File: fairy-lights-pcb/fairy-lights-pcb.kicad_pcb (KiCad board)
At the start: 2 copper layers, 59.5 x 59 mm, 16 parts, among them J1 Power_Jack, J2 Conn_LED_Strand, J3 Conn_LED_Strand, J4 Conn_Misc, J5 Conn_02x04_Top_Bottom, SW1 SW_PWR, SW2 SW_User, U1 WeMos_D1_mini, U2 TXS0108EPW

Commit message: Connect barrel jack mounting pin to ground
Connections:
- J1 pad 3: unconnected-(J1-MP-Pad3) -> GND

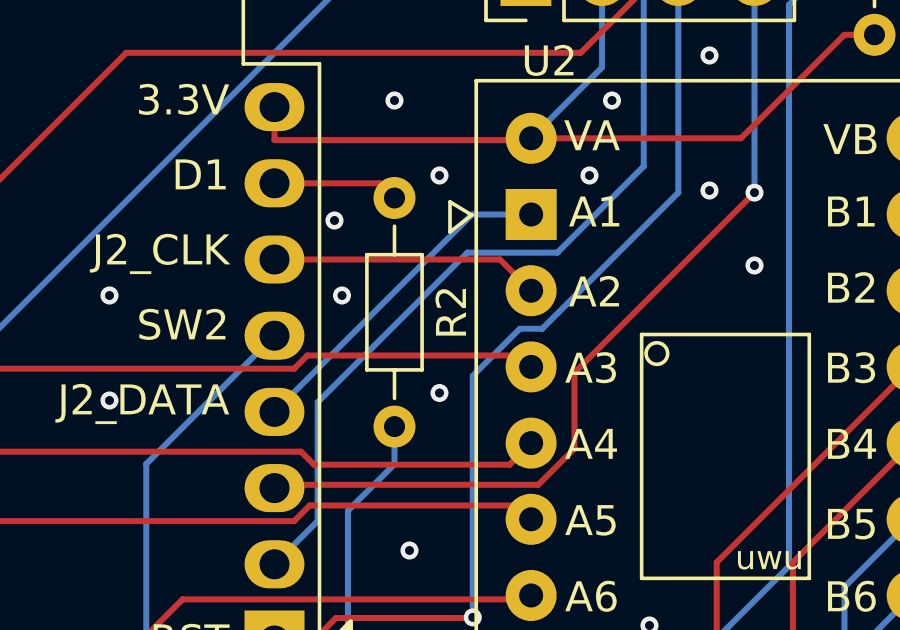
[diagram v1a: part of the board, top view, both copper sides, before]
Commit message: Update user LED resistor value
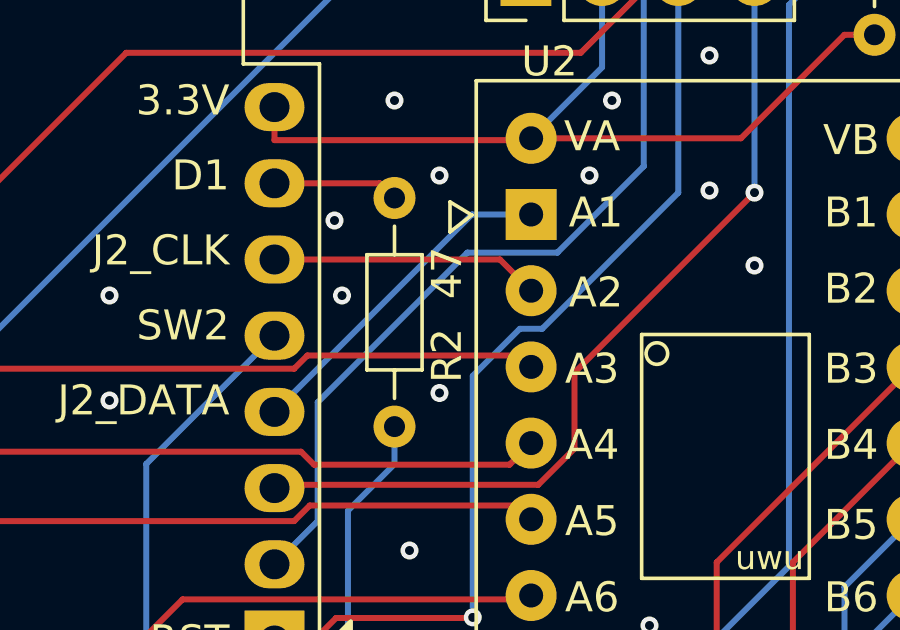
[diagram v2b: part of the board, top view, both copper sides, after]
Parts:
- R2: value TBD -> 47
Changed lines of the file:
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@@
 		(tags "Resistor Axial_DIN0204 series Axial Horizontal pin pitch 7.62mm 0.167W length 3.6mm diameter 1.6mm")
 		(property "Reference" "R2"
-			(at 3.81 -1.92 90)
+			(at 5.25 -1.75 90)
 			(layer "F.SilkS")
 			(effects
@@
 			)
 		)
-		(property "Value" "TBD"
-			(at 3.81 1.92 90)
-			(layer "F.Fab")
+		(property "Value" "47"
+			(at 2.5 -1.75 90)
+			(layer "F.SilkS")
 			(effects
 				(font

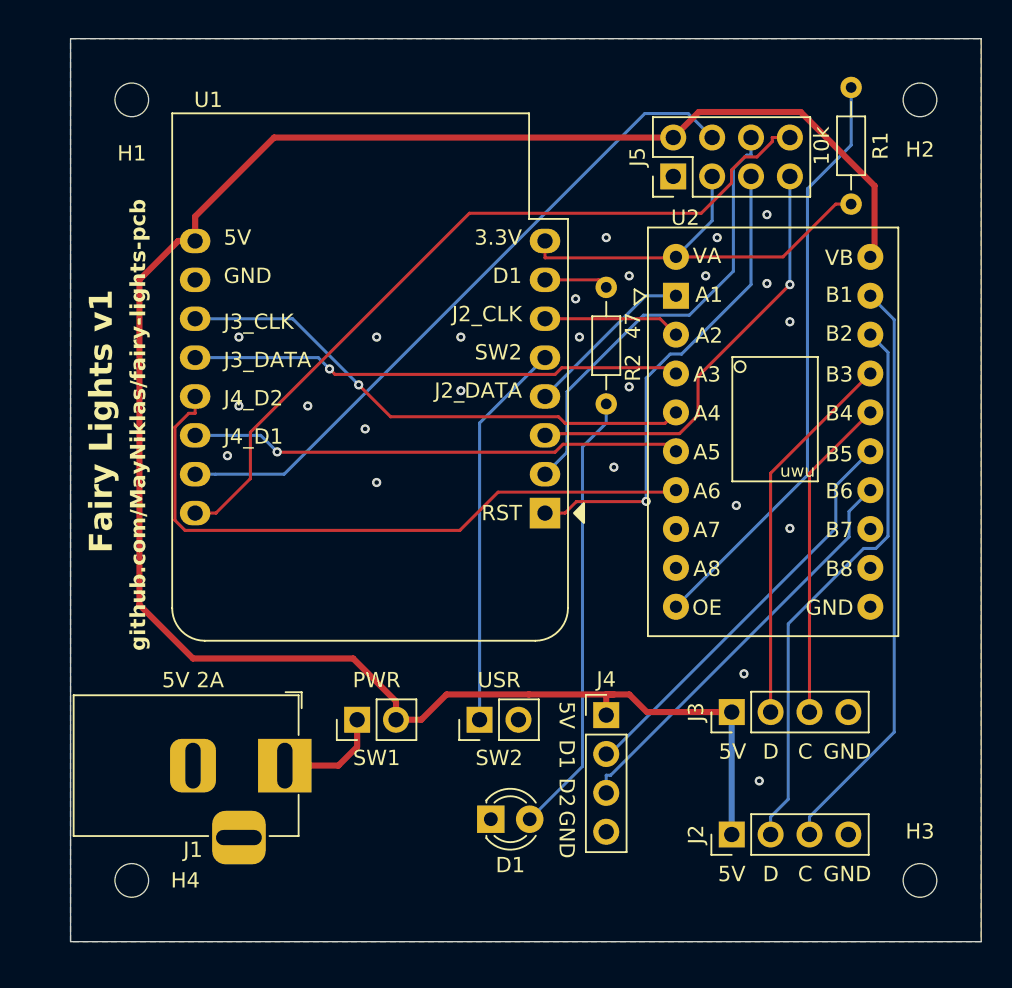
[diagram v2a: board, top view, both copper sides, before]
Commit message: Tweak board dimensions
They were *so close* to 6cm x 6cm, I couldn't (haha!) resist.
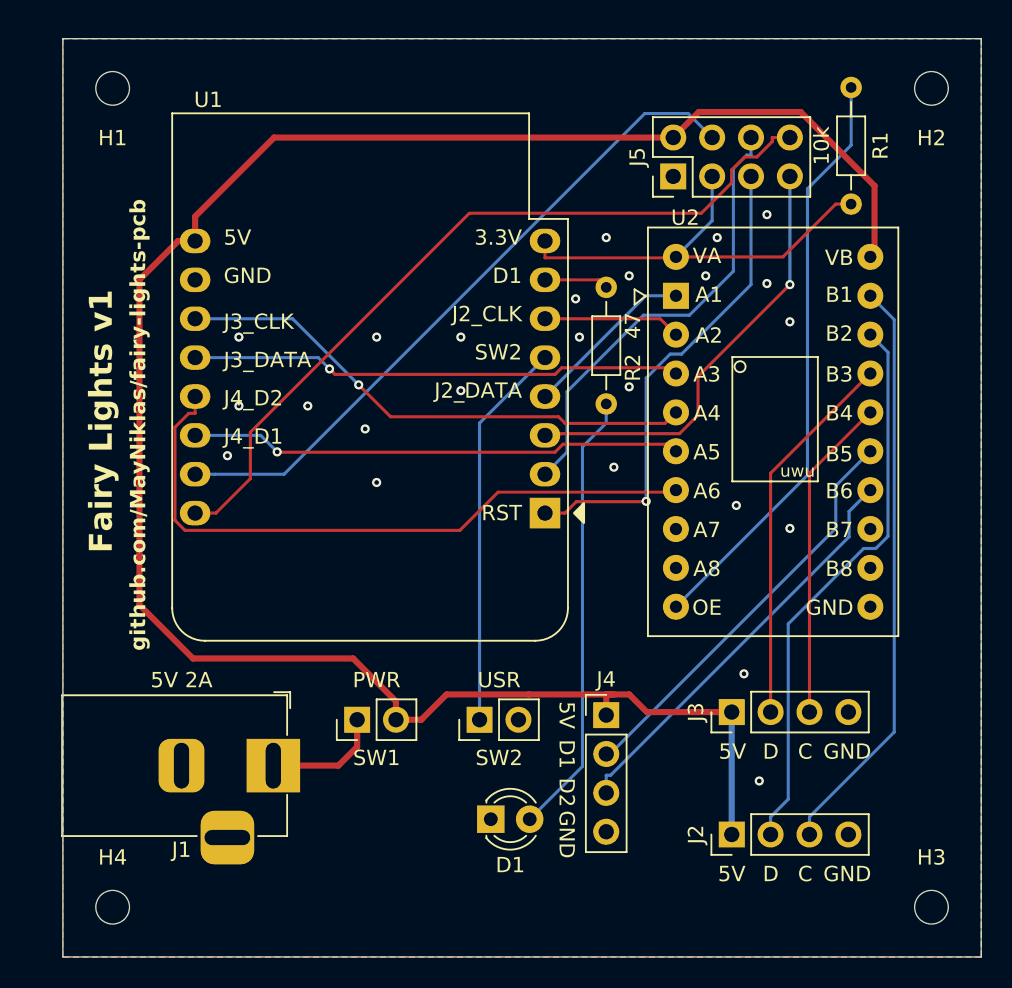
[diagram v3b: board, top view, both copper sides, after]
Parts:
- moved H4 2.15 mm to (65.2, 117.2)
- moved H3 1.90 mm to (118.8, 117.2)
- moved H1 1.46 mm to (65.2, 63.8)
- moved H2 1.06 mm to (118.8, 63.8)
- moved J1 0.75 mm to (75.8, 108.0)
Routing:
- net /5V_RAW: track 7.01 -> 7.76 mm
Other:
- board size 59.5 x 59 mm -> 60 x 60 mm
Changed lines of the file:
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@@
 	(footprint "Connector_BarrelJack:BarrelJack_Horizontal"
 		(layer "F.Cu")
-		(at 76.5 108)
+		(at 75.75 108)
 		(descr "DC Barrel Jack")
 		(tags "Power Jack")
@@
 	(footprint "MountingHole:MountingHole_2.2mm_M2"
 		(layer "F.Cu")
-		(at 118 115.5)
+		(at 118.75 117.25)
 		(descr "Mounting Hole 2.2mm, no annular, M2")
 		(tags "mounting hole 2.2mm no annular m2")
 		(property "Reference" "H3"
-			(at 0 -3.2 0)
+			(at 0 -3.25 0)
 			(layer "F.SilkS")
 			(effects
@@
 	(footprint "MountingHole:MountingHole_2.2mm_M2"
 		(layer "F.Cu")
-		(at 118 64.5)
+		(at 118.75 63.75)
 		(descr "Mounting Hole 2.2mm, no annular, M2")
 		(tags "mounting hole 2.2mm no annular m2")
@@
 	(footprint "MountingHole:MountingHole_2.2mm_M2"
 		(layer "F.Cu")
-		(at 66.5 64.5)
+		(at 65.25 63.75)
 		(descr "Mounting Hole 2.2mm, no annular, M2")
 		(tags "mounting hole 2.2mm no annular m2")
 		(property "Reference" "H1"
-			(at 0 3.5 0)
+			(at 0 3.25 0)
 			(layer "F.SilkS")
 			(effects
@@
 	(footprint "MountingHole:MountingHole_2.2mm_M2"
 		(layer "F.Cu")
-		(at 66.5 115.5)
+		(at 65.25 117.25)
 		(descr "Mounting Hole 2.2mm, no annular, M2")
 		(tags "mounting hole 2.2mm no annular m2")
 		(property "Reference" "H4"
-			(at 3.5 0 0)
+			(at 0 -3.25 0)
 			(layer "F.SilkS")
 			(effects
@@
 	)
 	(gr_rect
-		(start 62.5 60.5)
-		(end 122 119.5)
+		(start 62 60.5)
+		(end 122 120.5)
 		(stroke
 			(width 0.05)
@@
 	)
 	(gr_text "5V 2A"
-		(at 70.5 103 0)
+		(at 69.75 103 0)
 		(layer "F.SilkS")
 		(effects
@@
 	)
 	(segment
-		(start 80 108)
-		(end 76.5 108)
+		(start 81.225 106.775)
+		(end 80 108)
 		(width 0.4)
 		(layer "F.Cu")
@@
 	)
 	(segment
-		(start 81.225 106.775)
-		(end 80 108)
+		(start 80 108)
+		(end 75.75 108)
 		(width 0.4)
 		(layer "F.Cu")
@@
 		(polygon
 			(pts
-				(xy 62.5 60.5) (xy 122 60.5) (xy 122 119.5) (xy 62.5 119.5)
+				(xy 62 60.5) (xy 122 60.5) (xy 122 120.5) (xy 62 120.5)
 			)
 		)

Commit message: Align PCB edges to centimeter boundaries
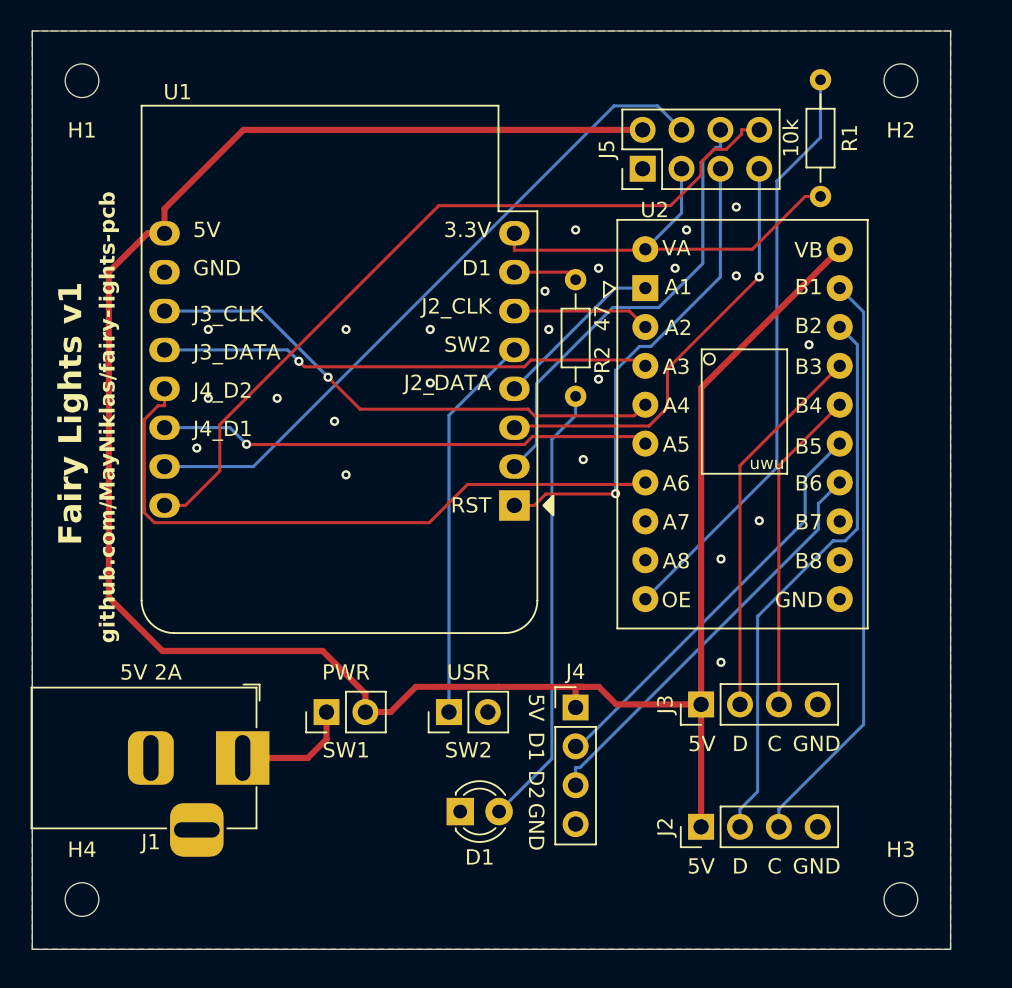
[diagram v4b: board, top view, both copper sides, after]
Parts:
- moved D1 2.06 mm to (88.0, 111.0)
- moved H1 2.06 mm to (63.2, 63.2)
- moved H2 2.06 mm to (116.8, 63.2)
- moved H3 2.06 mm to (116.8, 116.8)
- moved H4 2.06 mm to (63.2, 116.8)
- moved J1 2.06 mm to (73.8, 107.5)
- moved J2 2.06 mm to (103.7, 112.0)
- moved J3 2.06 mm to (103.7, 104.0)
- moved J4 2.06 mm to (95.5, 104.2)
- moved J5 2.06 mm to (99.9, 69.0)
- moved R1 2.06 mm to (111.5, 63.2)
- moved R2 2.06 mm to (95.5, 76.2)
- moved SW1 2.06 mm to (79.2, 104.5)
- moved SW2 2.06 mm to (87.2, 104.5)
- moved U1 2.06 mm to (91.5, 91.0)
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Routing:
- net +5V: track 135.0 -> 147.9 mm
- net GND: vias 24 -> 23
